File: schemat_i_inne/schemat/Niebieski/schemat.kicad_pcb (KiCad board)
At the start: 2 copper layers, 122.2 x 70.4 mm, 36 parts, among them J5 programming port, J6 USB_B_Micro, SW1 SW_DIP_x01, SW2 Home, SW3 triggerR, SW4 Select, SW5 triggerL, SW6 BumperL, SW7 BumperR, U1 ATmega1284P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

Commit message: better descriptive layer, and logo added
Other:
- board text added: "RetCon"
- board text added: "by KK"
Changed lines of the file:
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@@
     (property "Sheetfile" "schemat.kicad_sch")
     (property "Sheetname" "")
-    (fp_text reference "J1" (at 0 -0.5 unlocked) (layer "F.SilkS")
+    (fp_text reference "J1" (at 0 -0.5 unlocked) (layer "F.SilkS") hide
         (effects (font (size 1 1) (thickness 0.1)))
     )
     (fp_text value "~" (at 0 1 unlocked) (layer "F.Fab")
-        (effects (font (size 1 1) (thickness 0.15)))
-    )
-    (fp_text user "${REFERENCE}" (at 0 2.5 unlocked) (layer "F.Fab")
         (effects (font (size 1 1) (thickness 0.15)))
     )
@@
     (property "Sheetfile" "schemat.kicad_sch")
     (property "Sheetname" "")
-    (fp_text reference "J3" (at 0 -0.5 unlocked) (layer "F.SilkS")
+    (fp_text reference "J3" (at 0 -0.5 unlocked) (layer "F.SilkS") hide
         (effects (font (size 1 1) (thickness 0.1)))
     )
     (fp_text value "~" (at 0 1 unlocked) (layer "F.Fab")
-        (effects (font (size 1 1) (thickness 0.15)))
-    )
-    (fp_text user "${REFERENCE}" (at 0 2.5 unlocked) (layer "F.Fab")
         (effects (font (size 1 1) (thickness 0.15)))
     )
@@
     (property "Sheetfile" "schemat.kicad_sch")
     (property "Sheetname" "")
-    (fp_text reference "J2" (at 0 -0.5 unlocked) (layer "F.SilkS")
+    (fp_text reference "J2" (at 0 -0.5 unlocked) (layer "F.SilkS") hide
         (effects (font (size 1 1) (thickness 0.1)))
     )
     (fp_text value "~" (at 0 1 unlocked) (layer "F.Fab")
-        (effects (font (size 1 1) (thickness 0.15)))
-    )
-    (fp_text user "${REFERENCE}" (at 0 2.5 unlocked) (layer "F.Fab")
         (effects (font (size 1 1) (thickness 0.15)))
     )
@@
     (property "ki_keywords" "connector")
     (attr through_hole)
-    (fp_text reference "J5" (at 0 -2.77) (layer "F.SilkS")
-        (effects (font (size 1 1) (thickness 0.15)))
-    )
-    (fp_text value "programming port" (at 0 15.47) (layer "F.Fab")
+    (fp_text reference "J5" (at -3.023 14.707) (layer "F.SilkS")
+        (effects (font (size 1 1) (thickness 0.15)))
+    )
+    (fp_text value "programming port" (at -3.023 6.071 90) (layer "F.Fab")
         (effects (font (size 1 1) (thickness 0.15)))
     )
@@
     (property "Sheetfile" "schemat.kicad_sch")
     (property "Sheetname" "")
-    (fp_text reference "J4" (at 0 -0.5 unlocked) (layer "F.SilkS")
+    (fp_text reference "J4" (at 0 -0.5 unlocked) (layer "F.SilkS") hide
         (effects (font (size 1 1) (thickness 0.1)))
     )
     (fp_text value "~" (at 0 1 unlocked) (layer "F.Fab")
-        (effects (font (size 1 1) (thickness 0.15)))
-    )
-    (fp_text user "${REFERENCE}" (at 0 2.5 unlocked) (layer "F.Fab")
         (effects (font (size 1 1) (thickness 0.15)))
     )
@@
     (property "Sheetname" "")
     (attr through_hole)
-    (fp_text reference "RV1" (at -3.3 2.4) (layer "B.SilkS")
+    (fp_text reference "RV1" (at -7.426 -2.41) (layer "B.SilkS")
         (effects (font (size 1 1) (thickness 0.15)) (justify mirror))
     )
@@
     (property "ki_keywords" "TTL hex buffer OpenCol")
     (attr smd)
-    (fp_text reference "U5" (at 0 5.28 90) (layer "B.SilkS")
+    (fp_text reference "U5" (at 0 5.334 90) (layer "B.SilkS")
         (effects (font (size 1 1) (thickness 0.15)) (justify mirror))
     )
@@
     (property "ki_keywords" "inductor choke coil reactor magnetic")
     (attr smd)
-    (fp_text reference "L1" (at 0 4.45 90) (layer "B.SilkS")
+    (fp_text reference "L1" (at -3.302 -4.318 90) (layer "B.SilkS")
         (effects (font (size 1 1) (thickness 0.15)) (justify mirror))
     )
@@
     (property "ki_keywords" "quartz ceramic resonator oscillator")
     (attr smd)
-    (fp_text reference "Y1" (at 0 3.55 90) (layer "B.SilkS")
+    (fp_text reference "Y1" (at -0.254 3.55 90) (layer "B.SilkS")
         (effects (font (size 1 1) (thickness 0.15)) (justify mirror))
     )
@@
     (property "ki_keywords" "cap capacitor")
     (attr smd)
-    (fp_text reference "C5" (at 0 1.68 90) (layer "B.SilkS")
+    (fp_text reference "C5" (at -1.27 2.032 90) (layer "B.SilkS")
         (effects (font (size 1 1) (thickness 0.15)) (justify mirror))
     )
@@
     (property "ki_keywords" "R res resistor")
     (attr smd)
-    (fp_text reference "R1" (at 0 1.65) (layer "B.SilkS")
+    (fp_text reference "R1" (at 1.016 1.65) (layer "B.SilkS")
         (effects (font (size 1 1) (thickness 0.15)) (justify mirror))
     )
@@
     (property "Sheetname" "")
     (attr smd)
-    (fp_text reference "U6" (at 0 14.78) (layer "B.SilkS")
+    (fp_text reference "U6" (at 12.658 14.992) (layer "B.SilkS")
         (effects (font (size 1 1) (thickness 0.15)) (justify mirror))
     )
@@
     (property "ki_keywords" "R res resistor")
     (attr smd)
-    (fp_text reference "R3" (at 0 1.65) (layer "B.SilkS")
+    (fp_text reference "R3" (at -1.778 1.65) (layer "B.SilkS")
         (effects (font (size 1 1) (thickness 0.15)) (justify mirror))
     )
@@
     (property "ki_keywords" "R res resistor")
     (attr smd)
-    (fp_text reference "R4" (at 0 1.65) (layer "B.SilkS")
+    (fp_text reference "R4" (at 1.778 -1.524) (layer "B.SilkS")
         (effects (font (size 1 1) (thickness 0.15)) (justify mirror))
     )
@@
     (property "ki_keywords" "Voltage Regulator 1.5A Positive")
     (attr smd)
-    (fp_text reference "U2" (at 0 4.5 90) (layer "B.SilkS")
+    (fp_text reference "U2" (at 3.649 -4.573 90) (layer "B.SilkS")
         (effects (font (size 1 1) (thickness 0.15)) (justify mirror))
     )
@@
   (gr_rect (start 102.87 49.276) (end 225.044 119.634)
     (stroke (width 0.05) (type default)) (fill none) (layer "Edge.Cuts"))
+  (gr_text "RetCon" (at 208.28 113.284) (layer "F.SilkS")
+    (effects (font (size 3 3) (thickness 0.6) bold) (justify left bottom))
+  )
+  (gr_text "by KK" (at 215.392 116.332) (layer "F.SilkS")
+    (effects (font (size 1.5 1.5) (thickness 0.3) bold) (justify left bottom))
+  )
   (gr_text "Battery" (at 193.04 108.204 90) (layer "Dwgs.User")
     (effects (font (size 5 5) (thickness 0.3)) (justify left bottom))

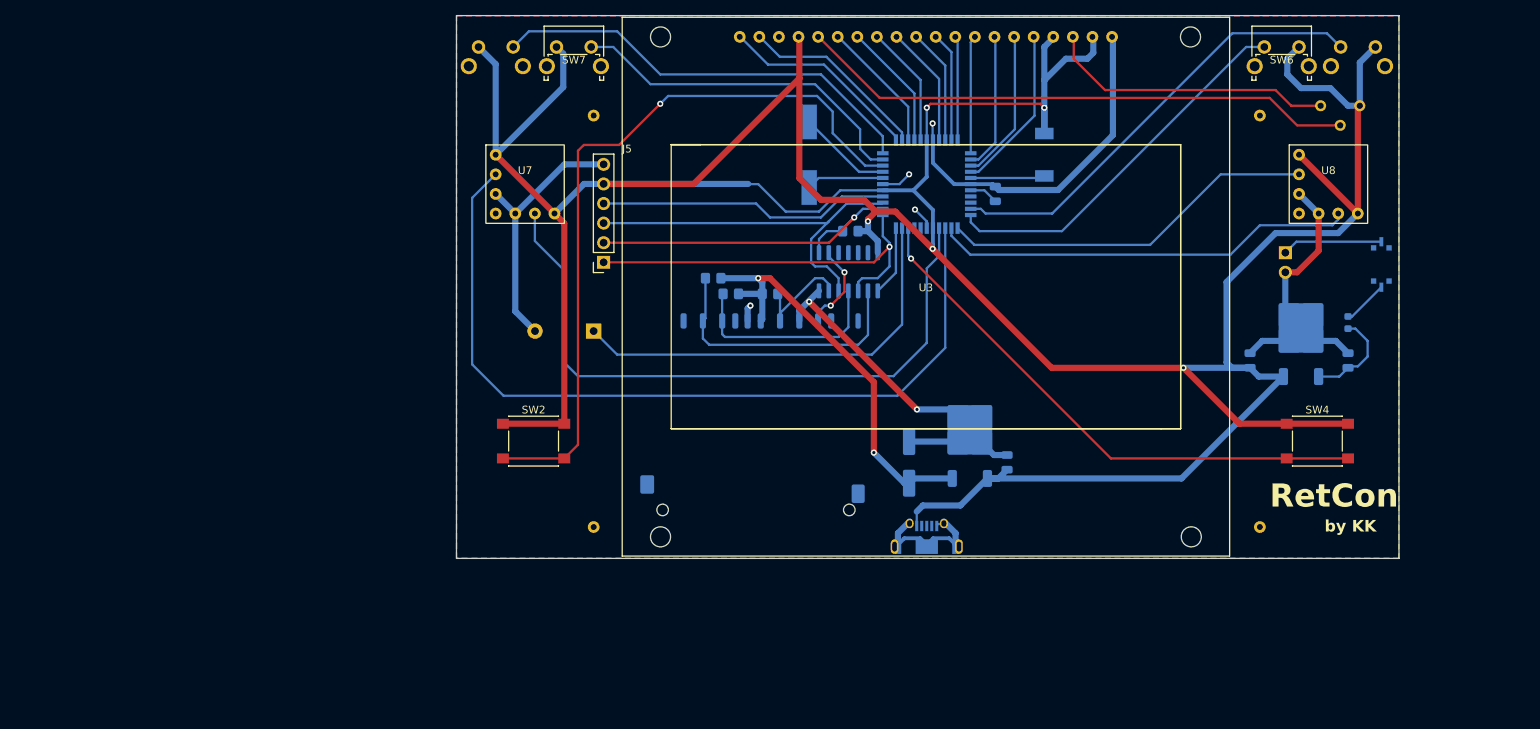
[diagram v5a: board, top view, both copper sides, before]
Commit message: Footprint for joysticks corrected
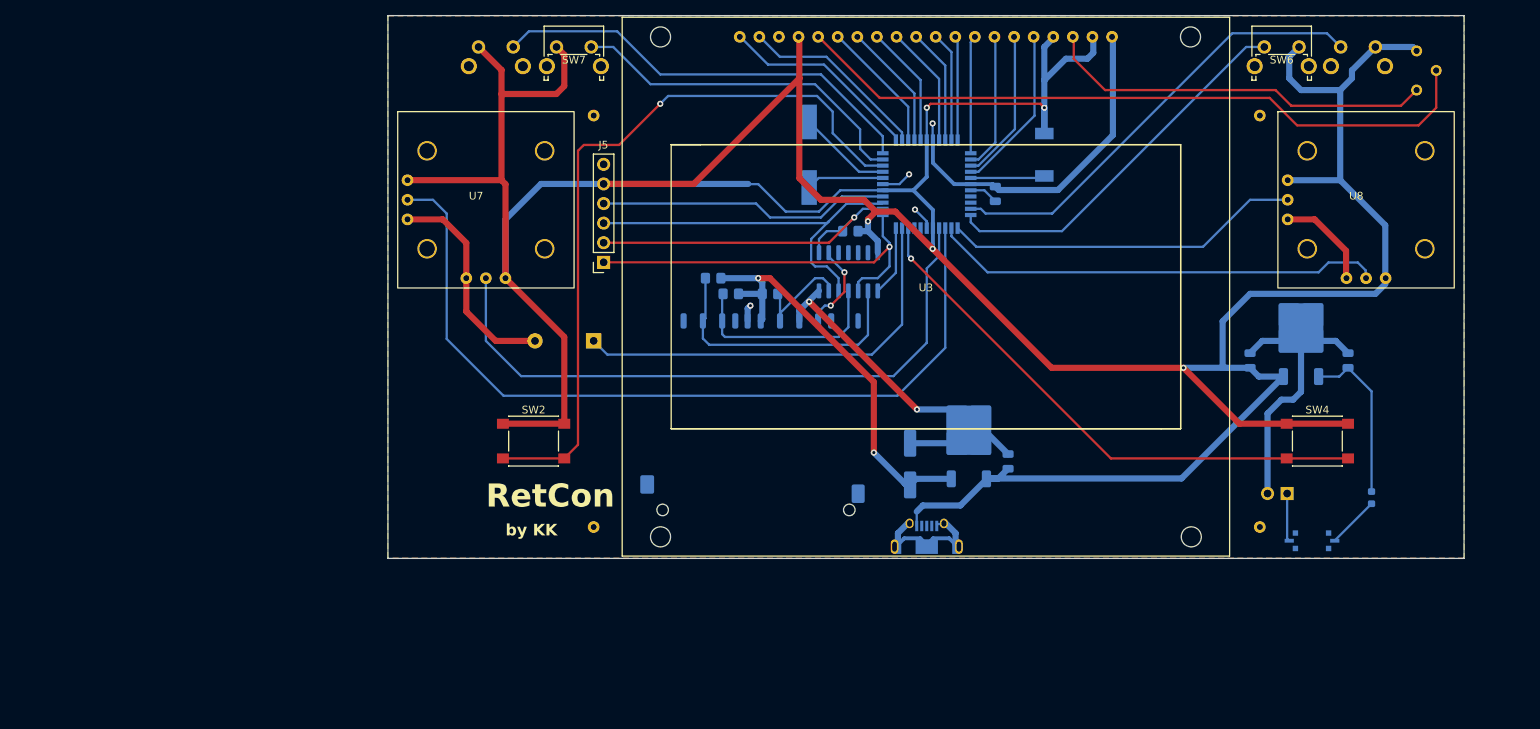
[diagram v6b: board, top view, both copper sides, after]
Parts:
- moved SW1 36.9 mm to (213.8, 117.3), turned to 180 degrees
- moved BT1 31.2 mm to (210.5, 111.2), turned to 90 degrees
- moved D1 22.9 mm to (221.5, 111.8), turned to -90 degrees
- moved RV1 12.6 mm to (227.3, 58.9), turned to -90 degrees
- moved U7 5.47 mm to (106.7, 73.2)
- moved U8 5.28 mm to (220.8, 73.2)
- moved BZ1 1.27 mm to (120.7, 91.4)
- moved C4 0.26 mm to (161.7, 107.4)
- moved C3 0.18 mm to (174.4, 107.1)
- moved U4 0.14 mm to (169.3, 104.3)
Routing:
- net +5V: track 489.4 -> 517.5 mm
- net Net-(U3-V0): track 72.3 -> 90.5 mm
- net Net-(U3-VEE): track 37.3 -> 50.6 mm
- net Net-(D1-K): track 12.7 -> 21.6 mm
- net GND: track 181.5 -> 190.2 mm
- net Net-(BT1-+): track 13.0 -> 6.23 mm
- net Net-(U1-PA2): track 54.8 -> 58.6 mm
- net Net-(U1-PA3): track 48.9 -> 46.3 mm
- net Net-(U1-PA0): track 85.9 -> 84.5 mm
- net Net-(D1-A): track 5.89 -> 6.78 mm
- net Net-(U1-PA1): track 107.0 -> 107.8 mm
- net +3V3: track 55.5 -> 56.2 mm
- net Net-(BZ1--): track 55.3 -> 54.8 mm
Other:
- board size 122.2 x 70.4 mm -> 139.5 x 70.4 mm

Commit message: More footprints updated - buttons - USB micro - coil
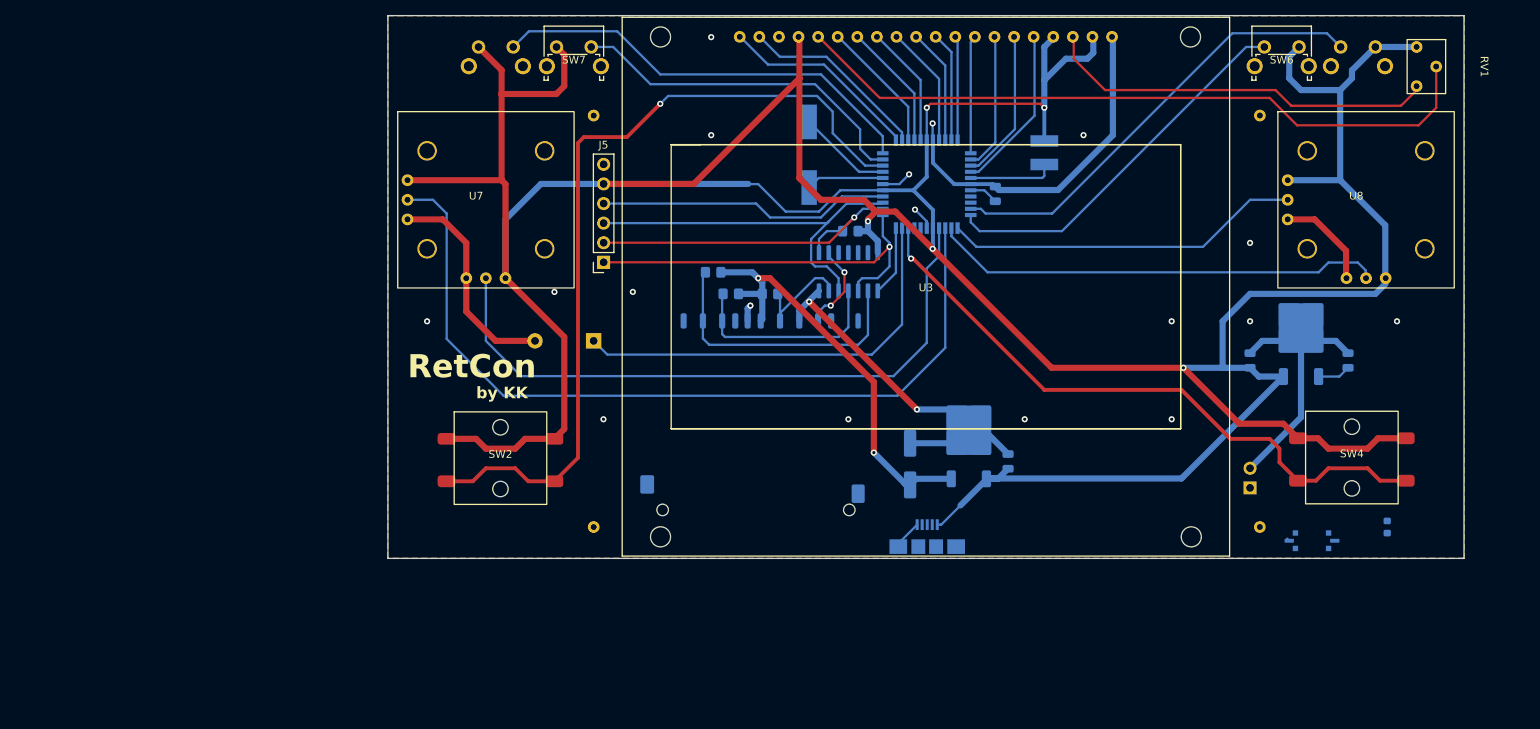
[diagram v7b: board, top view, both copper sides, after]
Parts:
- J6: footprint USB:microUSB -> Connector_USB:USB_Micro-B_Amphenol_10104110_Horizontal
- L1: footprint Inductor_SMD:L_6.3x6.3_H3 -> Inductor_SMD:L_Bourns-SRN4018
- RV1: footprint Potentiometer_THT:Potentiometer_Bourns_3296Z_Horizontal -> Blue:potentiometer10K; moved to F.Cu
- SW2, SW4: footprint Button_Switch_SMD:SW_Push_1P1T_NO_6x6mm_H9.5mm -> buttons:buttonSMD_withHoles
- moved SW4 4.96 mm to (218.9, 106.6)
- moved BT1 4.86 mm to (205.7, 110.5), turned to 0 degrees
- moved SW2 4.83 mm to (108.6, 106.6)
- moved D1 4.32 mm to (223.5, 115.6)
- moved RV1 3.30 mm to (228.6, 55.9)
- moved J6 1.30 mm to (163.9, 116.8)
- moved R2 0.76 mm to (136.1, 82.5)
- moved L1 0.25 mm to (179.1, 67.1)
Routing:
- net Net-(D1-K): track 21.6 -> 4.29 mm
- net GND: track 190.2 -> 173.6 mm, vias 6 -> 20
- net +5V: track 517.5 -> 530.0 mm
- net Net-(U1-PD0): track 96.4 -> 107.9 mm
- net Net-(U1-PB2): track 71.5 -> 82.5 mm
- net Net-(D1-A): track 6.78 -> 0.03 mm
- net Net-(BT1-+): track 6.23 -> 0.39 mm
- net Net-(U1-AVCC): track 9.65 -> 11.1 mm
- net Net-(U6-CD/DAT3): track 35.9 -> 36.7 mm
- net Net-(U3-V0): track 90.5 -> 91.0 mm
- net Net-(U3-VEE): track 50.6 -> 51.1 mm

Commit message: Fully updated PCB of RetCon
- It is in schemat/Niebieski folder
- First checkout of parts has been done
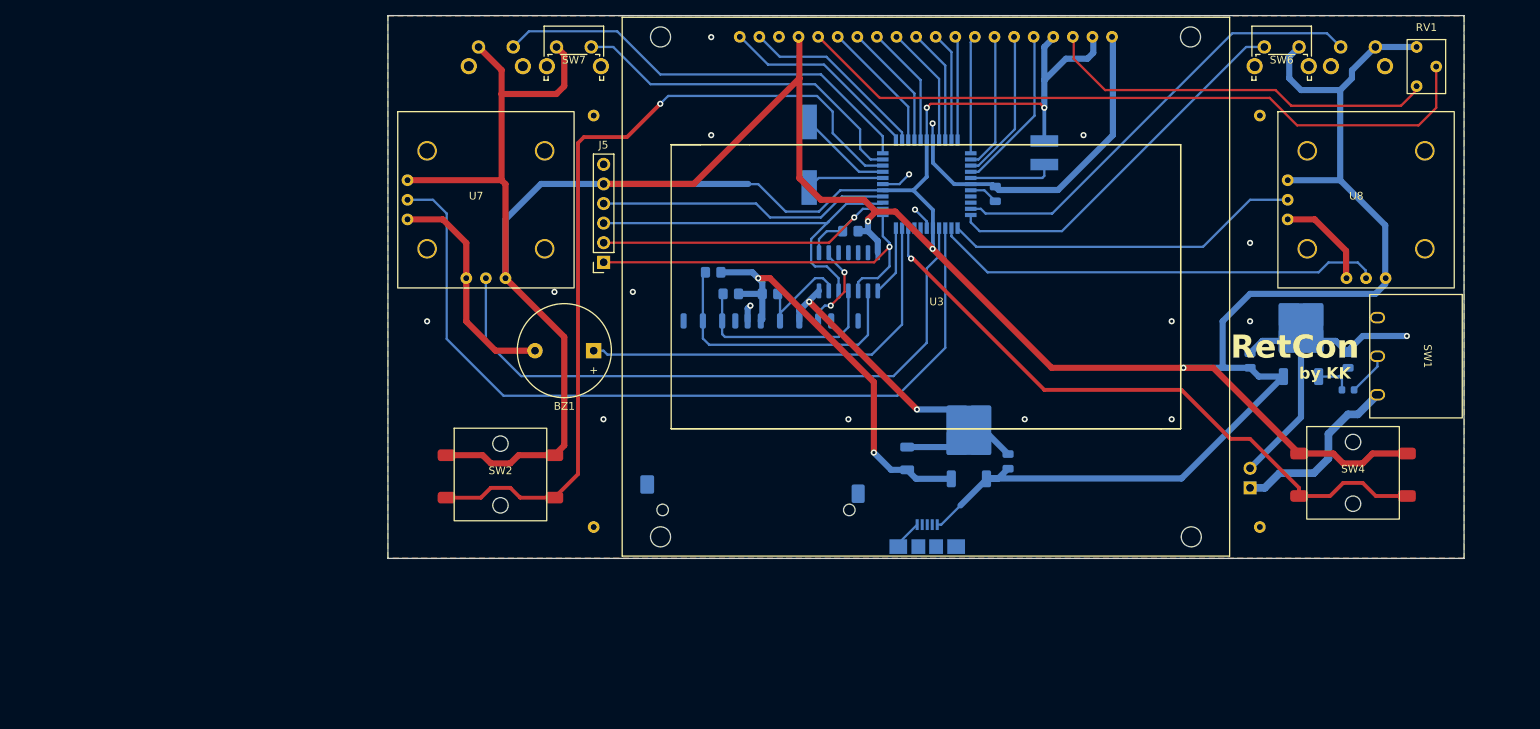
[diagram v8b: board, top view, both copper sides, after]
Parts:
- BZ1: moved to F.Cu
- C4: footprint Capacitor_SMD:CP_Elec_6.3x5.4_Nichicon -> Capacitor_SMD:C_1206_3216Metric
- J1: value ~ -> Hole1
- J2: value ~ -> Hole2
- J3: value ~ -> Hole3
- J4: value ~ -> Hole4
- J6: footprint Connector_USB:USB_Micro-B_Amphenol_10104110_Horizontal -> USB:USBMicro-SMD
- SW1: value SW_DIP_x01 -> SW_SPDT; footprint Button_Switch_SMD:SW_DIP_SPSTx01_Slide_Copal_CVS-01xB_W5.9mm_P1mm -> buttons:Button_Switch; moved to F.Cu
- moved J2 101.5 mm to (207.0, 115.6)
- moved J4 101.5 mm to (120.7, 62.2)
- moved SW1 28.0 mm to (228.2, 93.4), turned to -90 degrees
- moved D1 18.5 mm to (218.4, 97.8), turned to 0 degrees
- moved SW2 2.12 mm to (108.6, 108.8)
- moved SW4 1.99 mm to (219.1, 108.5)
- moved BZ1 1.27 mm to (120.7, 92.7)
- moved C4 0.82 mm to (161.3, 106.7)
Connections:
- SW1 pad 1: Net-(D1-A) -> unconnected-(SW1-A-Pad1)
- SW1 pad 2: Net-(BT1-+) -> Net-(D1-A)
- SW1 pad 3: (no net) -> Net-(BT1-+)
- U5 pad 10: (no net) -> unconnected-(U5-Pad10)
- U5 pad 11: (no net) -> unconnected-(U5-Pad11)
- U5 pad 12: (no net) -> unconnected-(U5-Pad12)
- U5 pad 13: (no net) -> unconnected-(U5-Pad13)
- U6 pad 10: (no net) -> unconnected-(U6-NC-Pad10)
- U6 pad 11: (no net) -> unconnected-(U6-NC-Pad11)
- U6 pad 12: (no net) -> unconnected-(U6-NC-Pad12)
- U6 pad 13: (no net) -> unconnected-(U6-NC-Pad13)
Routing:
- net Net-(BT1-+): track 0.39 -> 23.4 mm
- net GND: track 173.6 -> 186.4 mm
- net Net-(D1-A): track 0.03 -> 5.62 mm
- net +5V: track 530.0 -> 532.9 mm
- net Net-(D1-K): track 4.29 -> 6.15 mm
- net Net-(U1-PD0): track 107.9 -> 109.7 mm
- net +3V3: track 56.5 -> 55.2 mm
- net Net-(U1-PB2): track 82.5 -> 83.2 mm
- net Net-(BZ1--): track 54.8 -> 54.3 mm
